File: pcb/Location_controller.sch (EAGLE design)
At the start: 1 part

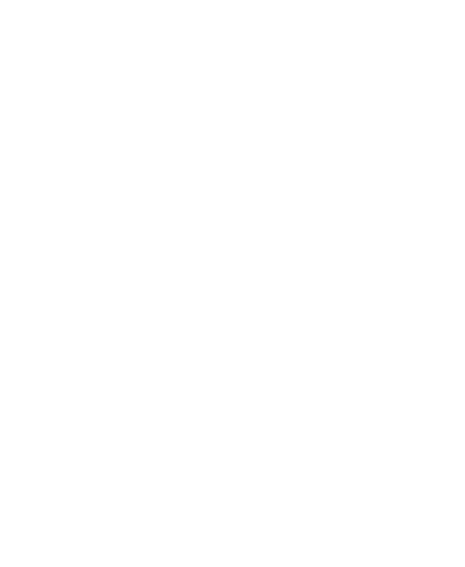
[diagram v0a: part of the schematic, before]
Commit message: Add crystal to layout
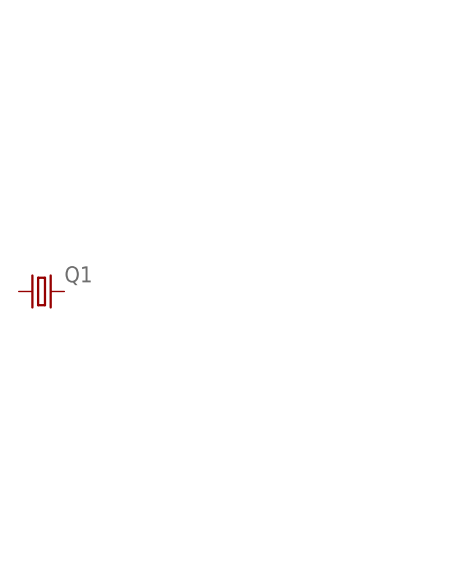
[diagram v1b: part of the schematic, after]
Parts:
- added Q1: (no value), crystal:CRYSTALHC49S
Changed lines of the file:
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@@
 <parts>
 <part name="U$1" library="stm32f4" deviceset="STM32F407V" device=""/>
+<part name="Q1" library="crystal" deviceset="CRYSTAL" device="HC49S"/>
 </parts>
 <sheets>
@@
 <instances>
 <instance part="U$1" gate="G$1" x="45.72" y="-12.7"/>
+<instance part="Q1" gate="G$1" x="-20.32" y="71.12"/>
 </instances>
 <busses>

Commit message: Add Crystal to Layout
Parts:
- added C1, C2: 20p, eagle-ltspice:C
- added R1: 0, eagle-ltspice:R
- added R2: 220, eagle-ltspice:R
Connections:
- new net GND: C1.2, C2.2
- new net N$1: C2.1, Q1.1, R2.1
- new net N$2: C1.1, Q1.2, R1.1
- new net OSC_IN: R1.2, U$1.PH0-OSC_IN(5T)
- new net OSC_OUT: R2.2, U$1.PH1-OSC_OUT(5T)
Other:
- moved on the sheet: Q1
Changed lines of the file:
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@@
 <layer number="97" name="Info" color="7" fill="1" visible="yes" active="yes"/>
 <layer number="98" name="Guide" color="6" fill="1" visible="yes" active="yes"/>
+<layer number="99" name="SpiceOrder" color="5" fill="1" visible="no" active="yes"/>
 <layer number="100" name="Muster" color="7" fill="1" visible="no" active="no"/>
 <layer number="101" name="Patch_Top" color="12" fill="4" visible="yes" active="yes"/>
@@
 <part name="U$1" library="stm32f4" deviceset="STM32F407V" device=""/>
 <part name="Q1" library="crystal" deviceset="CRYSTAL" device="HC49S"/>
+<part name="C1" library="eagle-ltspice" deviceset="C" device="" value="20p"/>
+<part name="C2" library="eagle-ltspice" deviceset="C" device="" value="20p"/>
+<part name="GND1" library="supply1" deviceset="GND" device=""/>
+<part name="GND2" library="supply1" deviceset="GND" device=""/>
+<part name="R1" library="eagle-ltspice" deviceset="R" device="" value="0"/>
+<part name="R2" library="eagle-ltspice" deviceset="R" device="" value="220"/>
 </parts>
 <sheets>
@@
 <instances>
 <instance part="U$1" gate="G$1" x="45.72" y="-12.7"/>
-<instance part="Q1" gate="G$1" x="-20.32" y="71.12"/>
+<instance part="Q1" gate="G$1" x="307.34" y="116.84"/>
+<instance part="C1" gate="G$1" x="320.04" y="93.98"/>
+<instance part="C2" gate="G$1" x="294.64" y="93.98"/>
+<instance part="GND1" gate="1" x="294.64" y="86.36"/>
+<instance part="GND2" gate="1" x="320.04" y="86.36"/>
+<instance part="R1" gate="G$1" x="320.04" y="121.92" rot="R90"/>
+<instance part="R2" gate="G$1" x="294.64" y="121.92" rot="R90"/>
 </instances>
 <busses>
 </busses>
 <nets>
+<net name="OSC_IN" class="0">
+<segment>
+<pinref part="U$1" gate="G$1" pin="PH0-OSC_IN(5T)"/>
+<wire x1="154.94" y1="2.54" x2="119.38" y2="2.54" width="0.1524" layer="91"/>
+<label x="149.86" y="2.54" size="1.778" layer="95"/>
+</segment>
+<segment>
+<pinref part="R1" gate="G$1" pin="2"/>
+<wire x1="320.04" y1="127" x2="320.04" y2="134.62" width="0.1524" layer="91"/>
+<label x="320.04" y="137.16" size="1.778" layer="95"/>
+</segment>
+</net>
+<net name="OSC_OUT" class="0">
+<segment>
+<pinref part="U$1" gate="G$1" pin="PH1-OSC_OUT(5T)"/>
+<wire x1="119.38" y1="0" x2="154.94" y2="0" width="0.1524" layer="91"/>
+<label x="149.86" y="0" size="1.778" layer="95"/>
+</segment>
+<segment>
+<pinref part="R2" gate="G$1" pin="2"/>
+<wire x1="294.64" y1="127" x2="294.64" y2="134.62" width="0.1524" layer="91"/>
+<label x="294.64" y="137.16" size="1.778" layer="95"/>
+</segment>
+</net>
+<net name="GND" class="0">
+<segment>
+<pinref part="C2" gate="G$1" pin="2"/>
+<pinref part="GND1" gate="1" pin="GND"/>
+</segment>
+<segment>
+<pinref part="C1" gate="G$1" pin="2"/>
+<pinref part="GND2" gate="1" pin="GND"/>
+</segment>
+</net>
+<net name="N$1" class="0">
+<segment>
+<pinref part="Q1" gate="G$1" pin="1"/>
+<pinref part="C2" gate="G$1" pin="1"/>
+<wire x1="304.8" y1="116.84" x2="294.64" y2="116.84" width="0.1524" layer="91"/>
+<wire x1="294.64" y1="116.84" x2="294.64" y2="96.52" width="0.1524" layer="91"/>
+<junction x="294.64" y="116.84"/>
+<pinref part="R2" gate="G$1" pin="1"/>
+</segment>
+</net>
+<net name="N$2" class="0">
+<segment>
+<pinref part="Q1" gate="G$1" pin="2"/>
+<pinref part="C1" gate="G$1" pin="1"/>
+<wire x1="309.88" y1="116.84" x2="320.04" y2="116.84" width="0.1524" layer="91"/>
+<wire x1="320.04" y1="116.84" x2="320.04" y2="96.52" width="0.1524" layer="91"/>
+<junction x="320.04" y="116.84"/>
+<pinref part="R1" gate="G$1" pin="1"/>
+</segment>
+</net>
 </nets>
 </sheet>

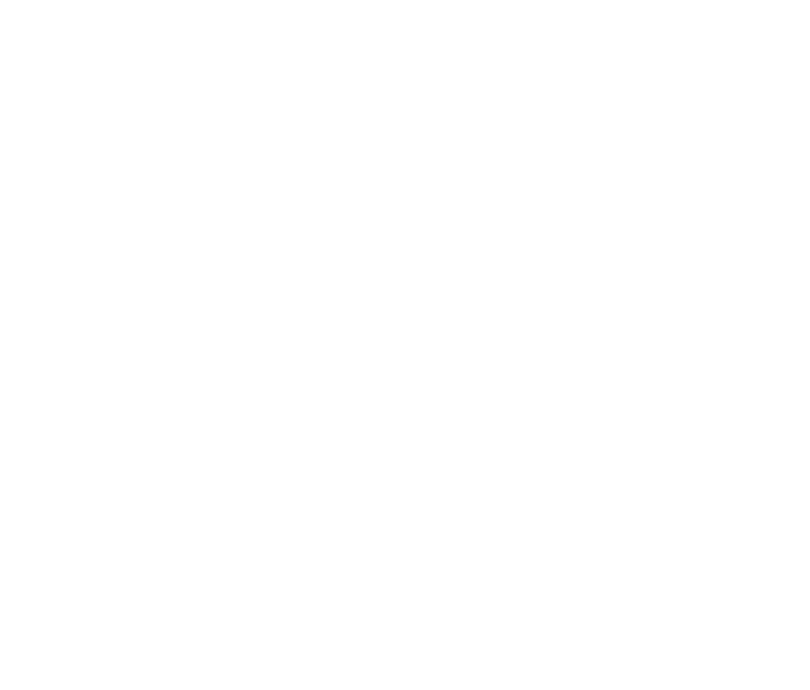
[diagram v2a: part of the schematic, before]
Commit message: Add Accelerometer to PCB
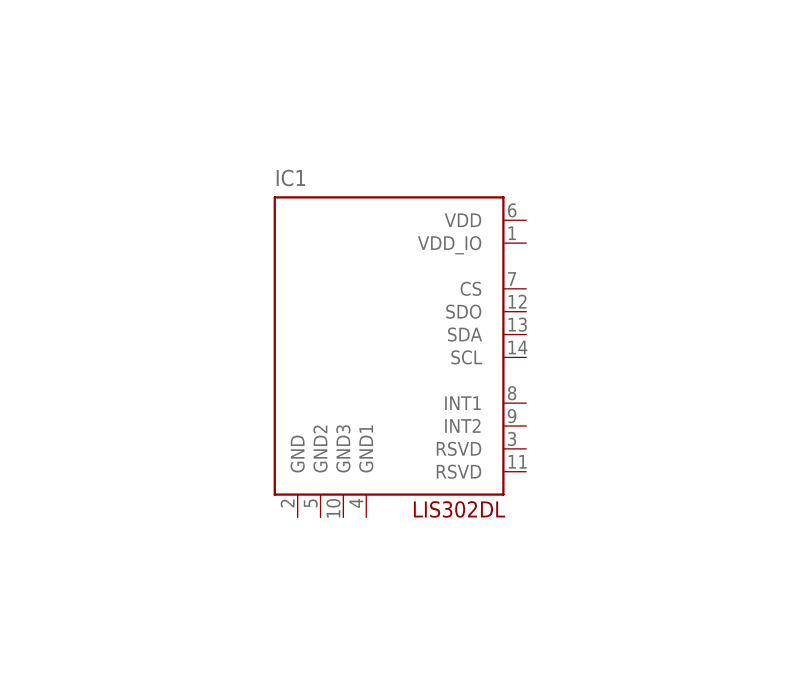
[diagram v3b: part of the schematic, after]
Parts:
- added IC1: LIS302DL, stm32f4:LSM303DLHC
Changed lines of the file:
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@@
 <part name="R1" library="eagle-ltspice" deviceset="R" device="" value="0"/>
 <part name="R2" library="eagle-ltspice" deviceset="R" device="" value="220"/>
+<part name="IC1" library="stm32f4" deviceset="LSM303DLHC" device="" value="LIS302DL"/>
 </parts>
 <sheets>
@@
 <instance part="R1" gate="G$1" x="320.04" y="121.92" rot="R90"/>
 <instance part="R2" gate="G$1" x="294.64" y="121.92" rot="R90"/>
+<instance part="IC1" gate="G$1" x="215.9" y="91.44"/>
 </instances>
 <busses>

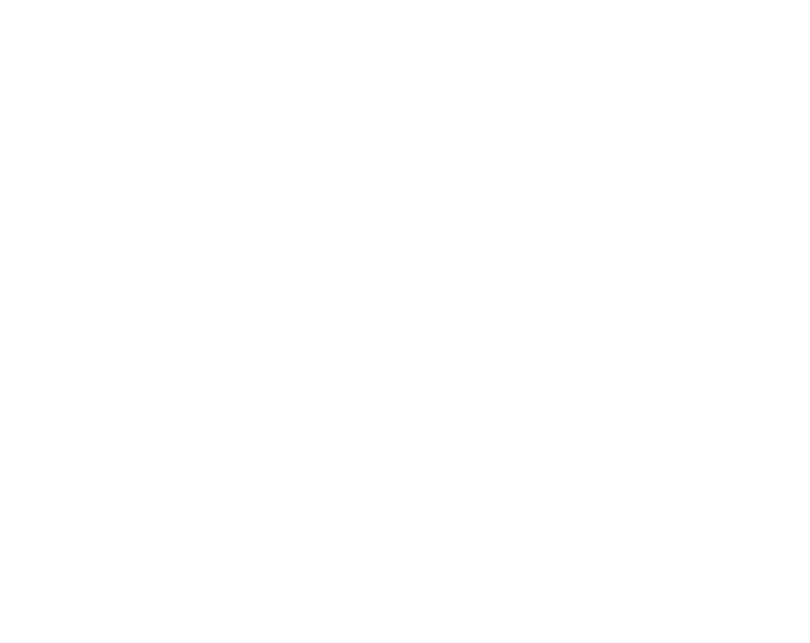
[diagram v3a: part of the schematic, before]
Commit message: Add Gyroscope to PCB
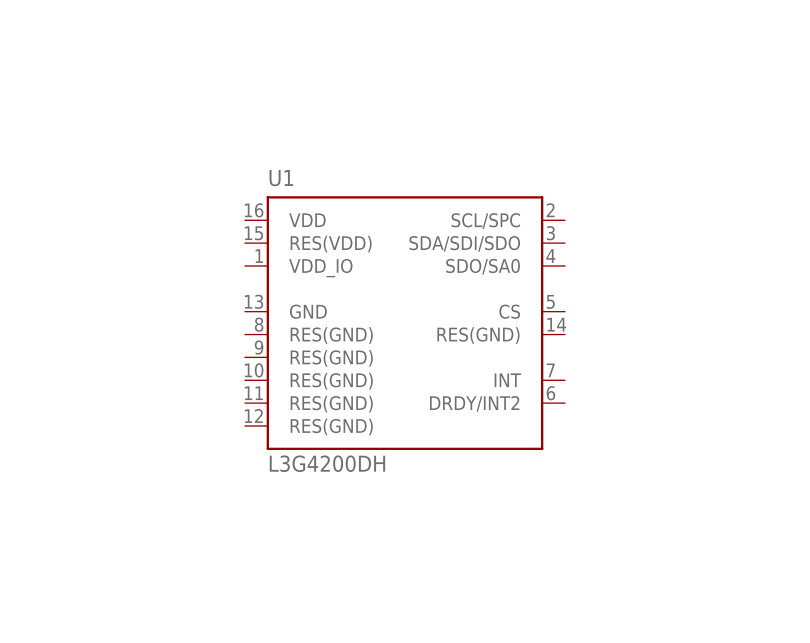
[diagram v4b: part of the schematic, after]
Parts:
- added U1: L3G4200DH, stm32f4:L3G4200DH
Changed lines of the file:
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@@
 <layer number="101" name="Patch_Top" color="12" fill="4" visible="yes" active="yes"/>
 <layer number="102" name="Vscore" color="7" fill="1" visible="yes" active="yes"/>
+<layer number="103" name="tMap" color="7" fill="1" visible="yes" active="yes"/>
 <layer number="104" name="Name" color="7" fill="1" visible="yes" active="yes"/>
+<layer number="105" name="tPlate" color="7" fill="1" visible="yes" active="yes"/>
+<layer number="106" name="bPlate" color="7" fill="1" visible="yes" active="yes"/>
+<layer number="107" name="Crop" color="7" fill="1" visible="yes" active="yes"/>
 <layer number="116" name="Patch_BOT" color="9" fill="4" visible="yes" active="yes"/>
 <layer number="121" name="_tsilk" color="7" fill="1" visible="yes" active="yes"/>
@@
 <layer number="201" name="201bmp" color="2" fill="1" visible="no" active="no"/>
 <layer number="202" name="202bmp" color="3" fill="1" visible="no" active="no"/>
+<layer number="203" name="203bmp" color="4" fill="10" visible="yes" active="yes"/>
+<layer number="204" name="204bmp" color="5" fill="10" visible="yes" active="yes"/>
+<layer number="205" name="205bmp" color="6" fill="10" visible="yes" active="yes"/>
+<layer number="206" name="206bmp" color="7" fill="10" visible="yes" active="yes"/>
+<layer number="207" name="207bmp" color="8" fill="10" visible="yes" active="yes"/>
+<layer number="208" name="208bmp" color="9" fill="10" visible="yes" active="yes"/>
 <layer number="250" name="Descript" color="3" fill="1" visible="no" active="no"/>
 <layer number="251" name="SMDround" color="12" fill="11" visible="no" active="no"/>
@@
 <part name="R2" library="eagle-ltspice" deviceset="R" device="" value="220"/>
 <part name="IC1" library="stm32f4" deviceset="LSM303DLHC" device="" value="LIS302DL"/>
+<part name="U1" library="stm32f4" deviceset="L3G4200DH*" device=""/>
 </parts>
 <sheets>
@@
 <instance part="R2" gate="G$1" x="294.64" y="121.92" rot="R90"/>
 <instance part="IC1" gate="G$1" x="215.9" y="91.44"/>
+<instance part="U1" gate="G$1" x="213.36" y="33.02"/>
 </instances>
 <busses>

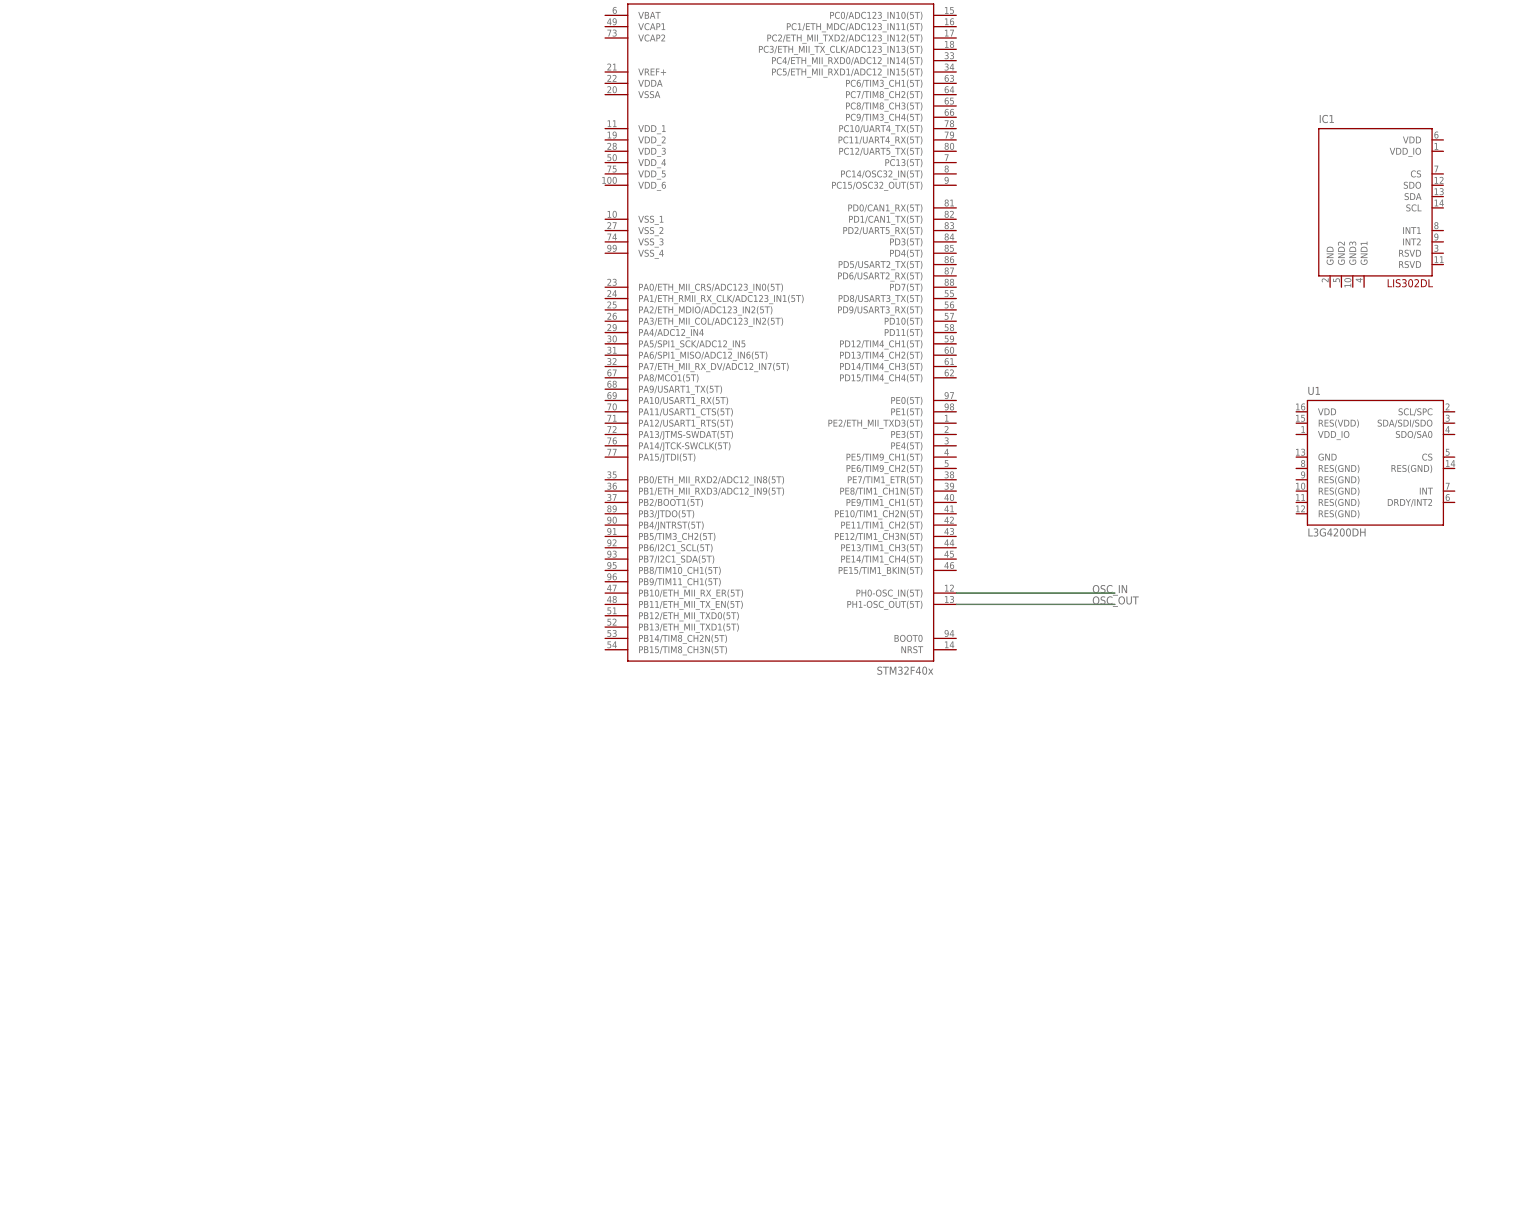
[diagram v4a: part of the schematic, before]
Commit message: Add Voltage Regulator and application circuits
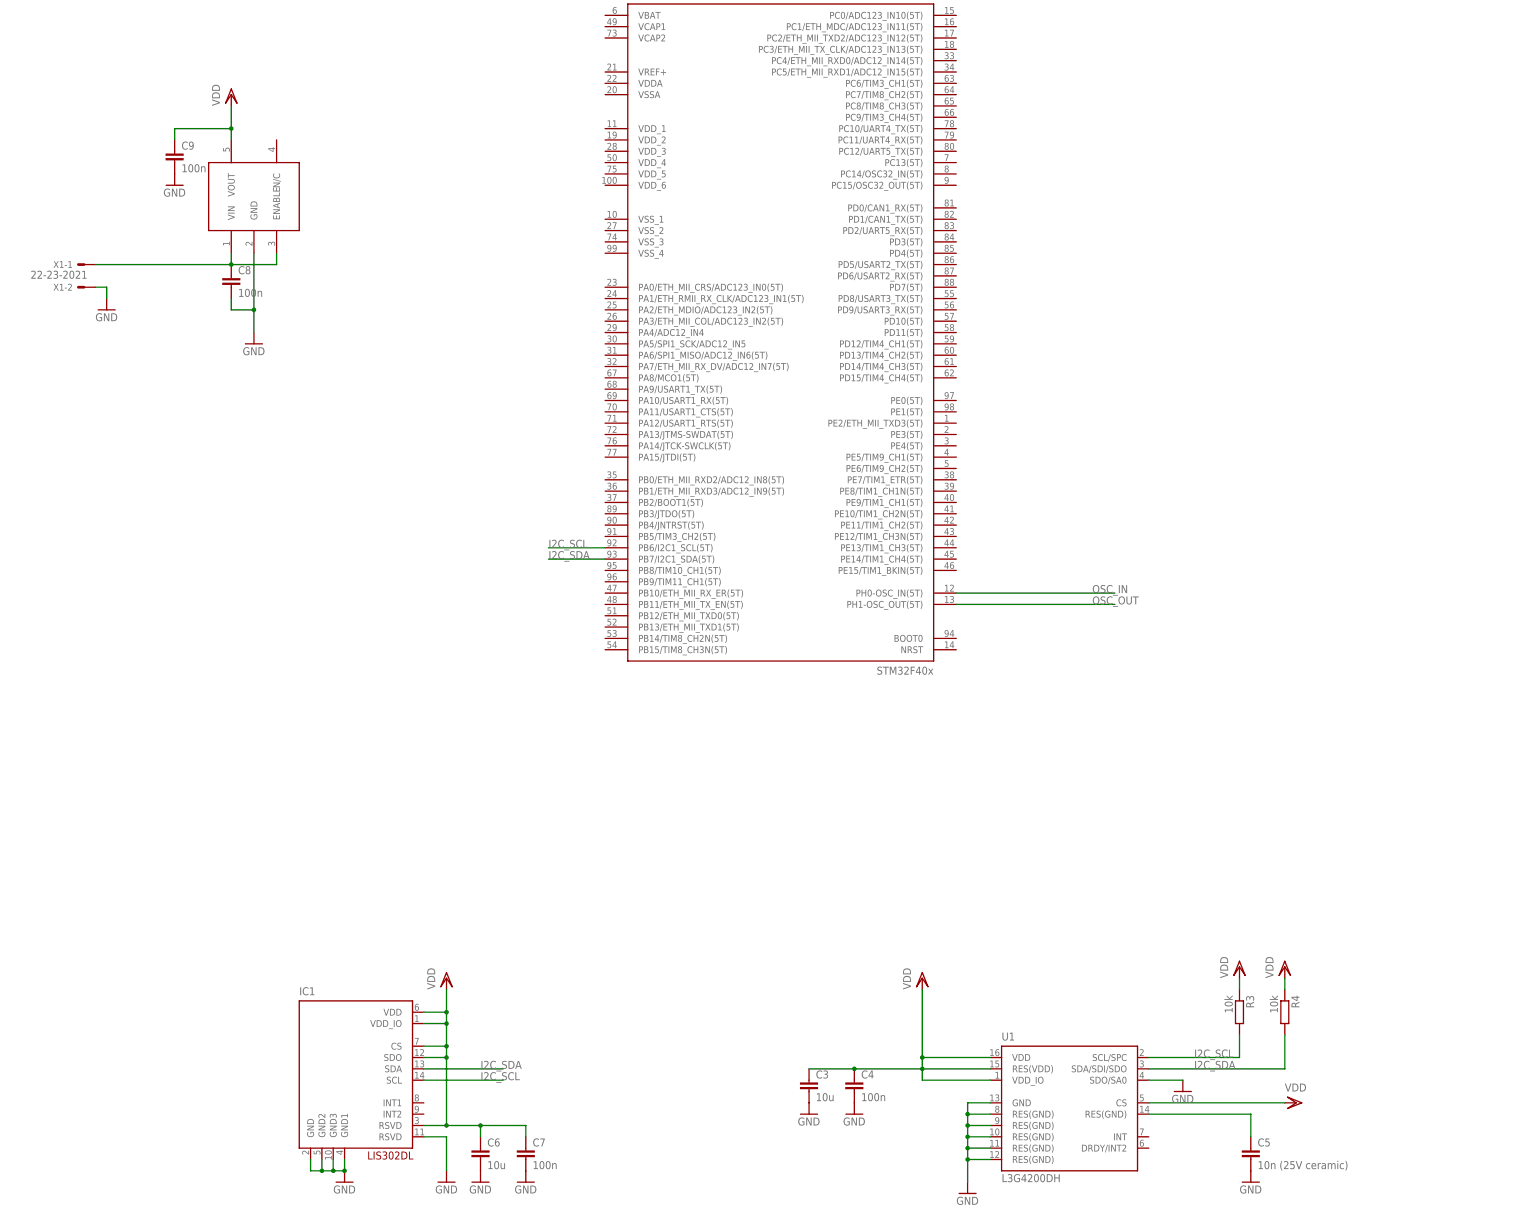
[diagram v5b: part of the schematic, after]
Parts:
- added C3, C6: 10u, eagle-ltspice:C
- added C4, C7, C8, C9: 100n, eagle-ltspice:C
- added C5: 10n (25V ceramic), eagle-ltspice:C
- added R3, R4: 10k, eagle-ltspice:R
- added U$2: NCP551, stm32f4:NCP551
- added X1: 22-23-2021, con-molex:22-23-2021
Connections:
- new net I2C_SCL: IC1.SCL, R3.2, U$1.PB6/I2C1_SCL(5T), U1.SCL/SPC
- new net I2C_SDA: IC1.SDA, R4.2, U$1.PB7/I2C1_SDA(5T), U1.SDA/SDI/SDO
- new net N$3: C5.1, U1.RES(GND)
- new net N$4: C8.1, U$2.ENABLE, U$2.VIN, X1-1.S
- new net VDD: C3.1, C4.1, C6.1, C7.1, C9.1, IC1.CS, IC1.RSVD@1, IC1.SDO, IC1.VDD, IC1.VDD_IO, R3.1, R4.1, U$2.VOUT, U1.CS, U1.RES(VDD), U1.VDD, U1.VDD_IO
- net GND: now also C3.2, C4.2, C5.2, C6.2, C7.2, C8.2, C9.2, IC1.GND, IC1.GND1, IC1.GND2, IC1.GND3, IC1.RSVD@2, U$2.GND, U1.GND, U1.RES(GND)@10, U1.RES(GND)@11, U1.RES(GND)@12, U1.RES(GND)@8, U1.RES(GND)@9, U1.SDO/SA0, X1-2.S
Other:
- moved on the sheet: IC1, U1

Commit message: Add decoupling to schematic + initial layout
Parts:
- removed U1: L3G4200DH, stm32f4:L3G4200DH
- added C10: 100n, eagle-ltspice:C
- added C11, C12, C13, C20, C21: 1u, eagle-ltspice:C
- added C14, C15, C16, C17, C18, C19, C22, C23: 10n, eagle-ltspice:C
- added C24, C25: 2.2u, eagle-ltspice:C
- added JP2: (no value), pinhead:PINHD-1X20
- added POWER: (no value), pinhead:PINHD-1X3
- C3: value 10u -> 1u
- C4: value 100n -> 1u
- C5: value 10n (25V ceramic) -> 1u
- renumbered U$2 to REG
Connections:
- removed net N$3: C5.1, U1.RES(GND)
- new net N$10: C9.1, POWER.1, REG.VOUT
- new net N$5: C10.1, U$1.NRST
- new net N$8: C25.1, U$1.VCAP1
- new net N$9: C24.1, U$1.VCAP2
- net GND: now also C10.2, C11.2, C12.2, C13.2, C14.2, C15.2, C16.2, C17.2, C18.2, C19.2, C20.2, C21.2, C22.2, C23.2, C24.2, C25.2, U$1.VSSA, U$1.VSS_1, U$1.VSS_2, U$1.VSS_3, U$1.VSS_4; no longer U1.GND, U1.RES(GND)@10, U1.RES(GND)@11, U1.RES(GND)@12, U1.RES(GND)@8, U1.RES(GND)@9, U1.SDO/SA0
- net I2C_SCL: now also R4.2; no longer R3.2, U1.SCL/SPC
- net I2C_SDA: now also R3.2; no longer R4.2, U1.SDA/SDI/SDO
- net VDD: now also C11.1, C12.1, C13.1, C14.1, C15.1, C16.1, C17.1, C18.1, C19.1, C20.1, C21.1, C22.1, C23.1, C5.1, POWER.2, U$1.VDDA, U$1.VDD_1, U$1.VDD_2, U$1.VDD_3, U$1.VDD_4, U$1.VDD_5, U$1.VDD_6, U$1.VREF+; no longer C9.1, REG.VOUT, U1.CS, U1.RES(VDD), U1.VDD, U1.VDD_IO
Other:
- note added: "Accelerometer"
- note added: "Antenna Controller + Support"
- note added: "Decoupling 1u // 10n"
- note added: "Jumper selector"
- moved on the sheet: C1, C2, C3, C4, C5, C6, C7, IC1, Q1, R1, R2, R3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
